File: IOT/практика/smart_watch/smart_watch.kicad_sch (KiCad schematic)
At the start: 30 parts, among them J1 Conn_01x02_Pin, J2 USB_C_Receptacle_USB2.0_16P, SW2 SW_Push, U1 WeMos_D1_mini, U3 KXTJ3-1057, U4 MAX30102, U5 TPS61230DRC, U6 BQ24090DGQ

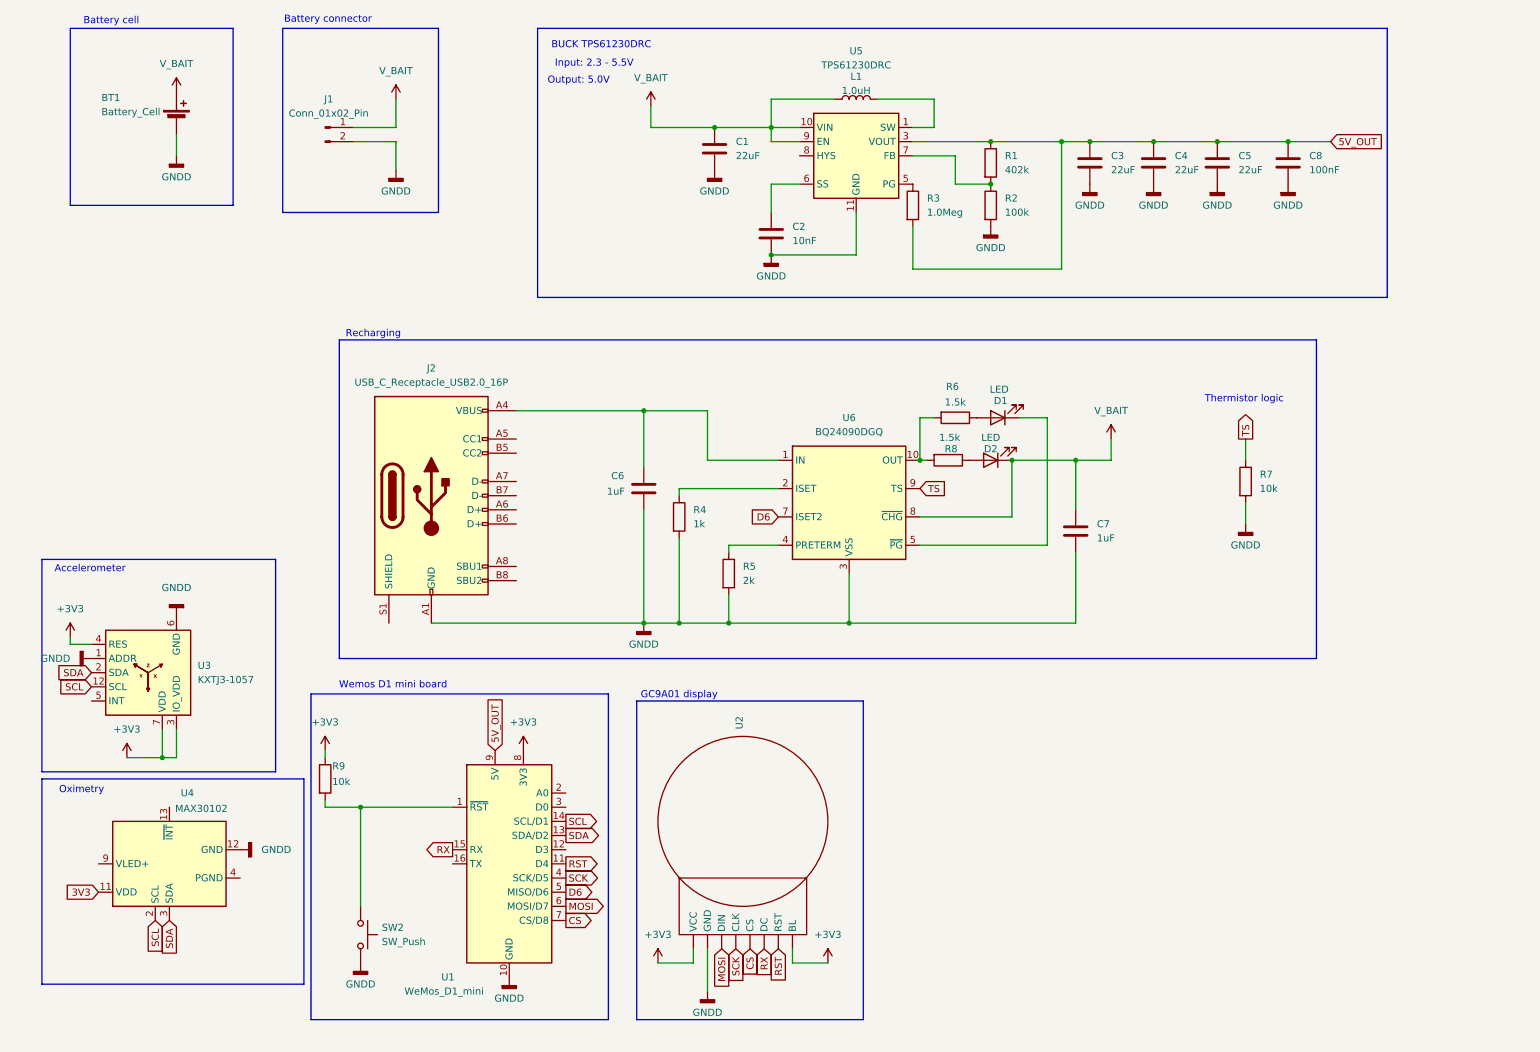
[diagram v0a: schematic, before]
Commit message: feat: adding hws and iot
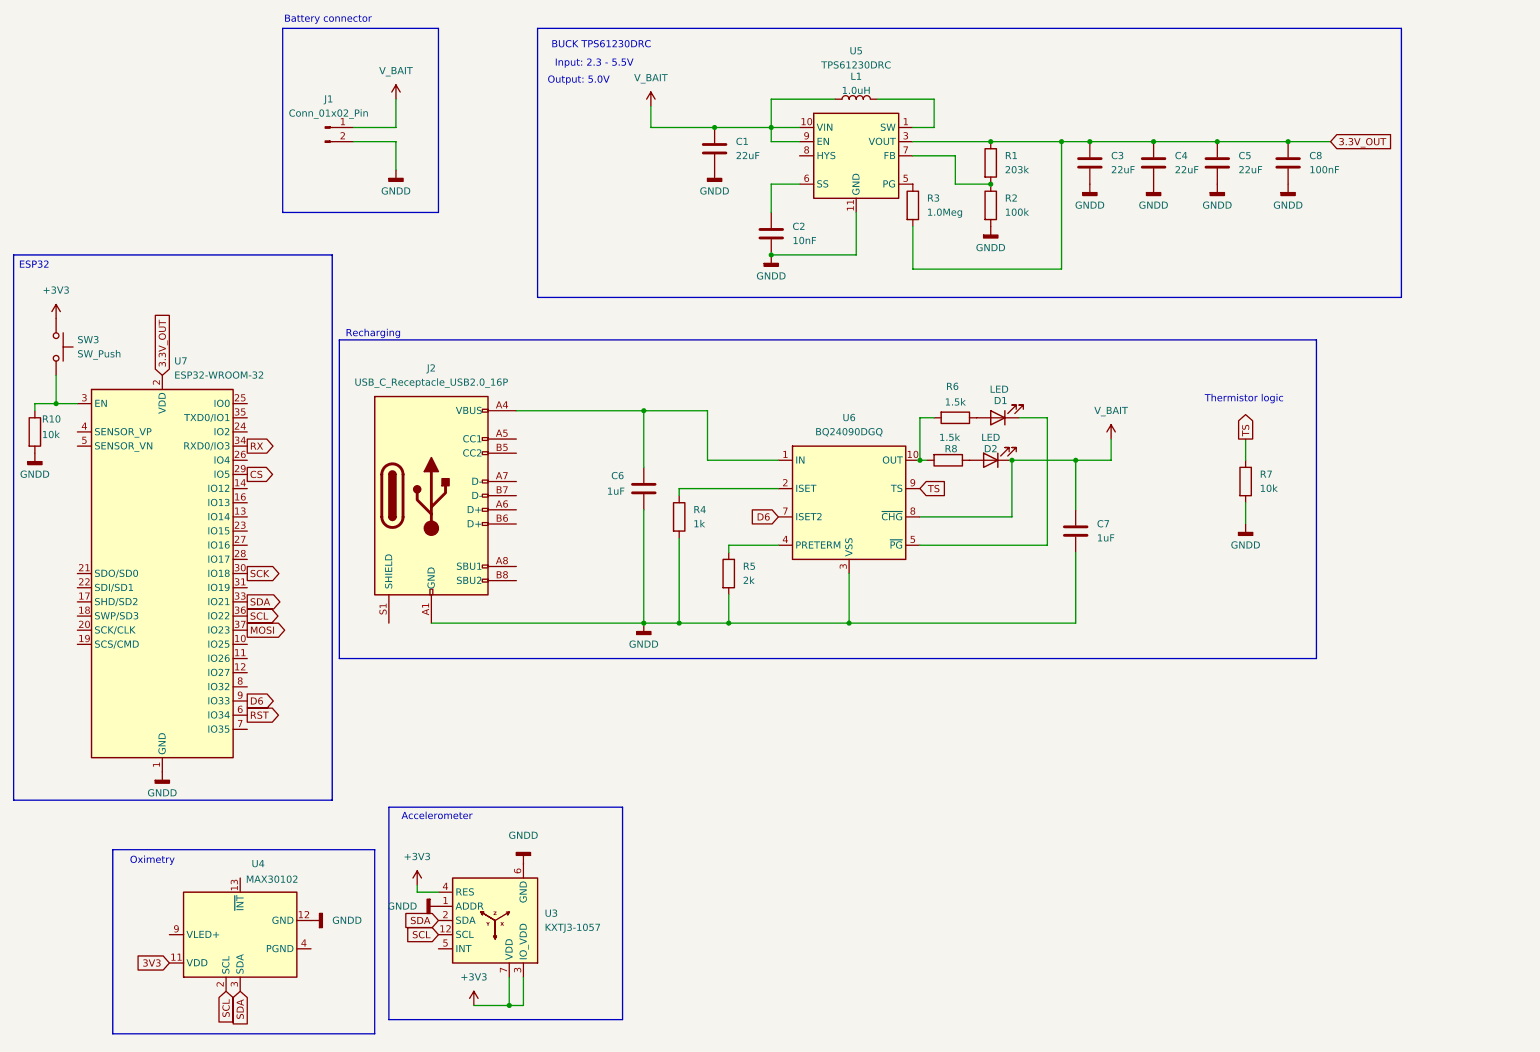
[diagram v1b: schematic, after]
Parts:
- removed BT1: Battery_Cell, symbol Device:Battery_Cell
- removed R9: 10k, Resistor_SMD:R_0402_1005Metric, symbol Device:R
- removed SW2: SW_Push, Button_Switch_SMD:SW_Push_1P1T_NO_CK_KMR2, symbol Switch:SW_Push
- removed U1: WeMos_D1_mini, Module:WEMOS_D1_mini_light, symbol MCU_Module:WeMos_D1_mini
- removed U2: ~, symbol circle_oled:Circle_OLED_gc9a01
- added R10: 10k, Resistor_SMD:R_0603_1608Metric, symbol Device:R
- added SW3: SW_Push, Button_Switch_SMD:SW_Push_1P1T_NO_CK_KMR2, symbol Switch:SW_Push
- added U7: ESP32-WROOM-32, RF_Module:ESP32-WROOM-32, symbol RF_Module:ESP32-WROOM-32
- C1, C2, C3, C4, C5, C6, C7, C8: footprint Capacitor_SMD:C_0805_2012Metric -> Capacitor_SMD:C_0603_1608Metric
- D1, D2: footprint LED_SMD:LED_0201_0603Metric -> LED_SMD:LED_0603_1608Metric
- J1: footprint (none) -> TerminalBlock:TerminalBlock_MaiXu_MX126-5.0-02P_1x02_P5.00mm
- L1: footprint Inductor_SMD:L_Coilcraft_LPS3314 -> Inductor_SMD:L_Changjiang_FXL0630
- R1: value 402k -> 203k; footprint Resistor_SMD:R_0402_1005Metric -> Resistor_SMD:R_0603_1608Metric
- R2, R3, R4, R5, R6, R7, R8: footprint Resistor_SMD:R_0402_1005Metric -> Resistor_SMD:R_0603_1608Metric
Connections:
- net +3V3: now also SW3.1
- net CS: now also U7.29 (IO5)
- net D6: now also U7.9 (IO33)
- net GNDD: now also R10.2, U7.1 (GND), U7.15 (GND), U7.38 (GND), U7.39 (GND)
- net MOSI: now also U7.37 (IO23)
- net RST: now also U7.6 (IO34)
- net RX: now also U7.34 (RXD0/IO3)
- net SCK: now also U7.30 (IO18)
- net SCL: now also U7.36 (IO22)
- net SDA: now also U7.33 (IO21)
- net 5V_OUT renamed 3.3V_OUT
- net 3.3V_OUT: now also U7.2 (VDD)
- new net: R10.1, SW3.2, U7.3 (EN)
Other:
- note removed: "Battery cell"
- note removed: "GC9A01 display"
- note removed: "Wemos D1 mini board"
- moved on the sheet: U3, U4

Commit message: feat: adding things
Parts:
- added U1: ~, Connector_FFC:Hirose_FH12-13S-0.5SH_1x13-1MP_P0.50mm_Horizontal, symbol FH12-13S-0.5SH(55):FH12-13S-0.5SH(55)
- added U2: MAX17261xxWL, Package_BGA:Maxim_WLP-9_1.595x1.415_Layout3x3_P0.4mm_Ball0.27mm_Pad0.25mm_NSMD, symbol Battery_Management:MAX17261xxWL
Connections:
- net 3.3V_OUT: now also U1.1
- net GNDD: now also U1.2, U1.MP
- net MOSI: now also U1.4
- net SCK: now also U1.5
- net SCL: now also U1.11
- net SDA: now also U1.10
- net LCD_BL: now reaches U7.13 (IO14)
- net LCD_BL: now also U1.9
- net LCD_DC: now reaches U7.14 (IO12)
- net LCD_DC: now also U1.7
- net LCD_RST: now reaches U7.16 (IO13)
- net LCD_RST: now also U1.8
- net TP_INT: now reaches U7.23 (IO15)
- net TP_INT: now also U1.12
- net TP_RST: now reaches U7.27 (IO16)
- net TP_RST: now also U1.13
- net MISO: now reaches U7.31 (IO19)
- net MISO: now also U1.3
- net CS renamed LCD_CS
- net LCD_CS: now also U1.6

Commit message: feat: adding things
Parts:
- removed U2: MAX17261xxWL, Package_BGA:Maxim_WLP-9_1.595x1.415_Layout3x3_P0.4mm_Ball0.27mm_Pad0.25mm_NSMD, symbol Battery_Management:MAX17261xxWL
- added U8: LC709203FQH-01TWG, Package_DFN_QFN:WDFN-8-1EP_4x3mm_P0.65mm_EP2.4x1.8mm, symbol Battery_Management:LC709203FQH-01TWG
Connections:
- net +3V3: now also R10.1; no longer SW3.1
- net GNDD: now also SW3.1; no longer R10.2
- net at SW3.2, U7.3 (EN): now also R10.2; no longer R10.1
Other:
- moved on the sheet: R10, SW3
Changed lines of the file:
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@@
 	(wire
 		(pts
+			(xy 16.51 100.33) (xy 16.51 105.41)
+		)
+		(stroke
+			(width 0)
+			(type default)
+		)
+	)
+	(wire
+		(pts
 			(xy 200.66 59.69) (xy 200.66 36.83)
 		)
@@
 	(wire
 		(pts
-			(xy 16.51 83.82) (xy 16.51 85.09)
-		)
-		(stroke
-			(width 0)
-			(type default)
-		)
-	)
-	(wire
-		(pts
 			(xy 175.26 86.36) (xy 175.26 93.98)
 		)
@@
 	(wire
 		(pts
-			(xy 20.32 78.74) (xy 20.32 83.82)
+			(xy 20.32 76.2) (xy 20.32 83.82)
 		)
 		(stroke
@@
 	(wire
 		(pts
+			(xy 16.51 83.82) (xy 16.51 90.17)
+		)
+		(stroke
+			(width 0)
+			(type default)
+		)
+	)
+	(wire
+		(pts
 			(xy 149.86 99.06) (xy 132.08 99.06)
 		)
@@
 	(symbol
 		(lib_id "Device:R")
-		(at 16.51 88.9 0)
+		(at 20.32 72.39 0)
 		(unit 1)
 		(exclude_from_sim no)
@@
 		(dnp no)
 		(property "Reference" "R10"
-			(at 17.78 86.614 0)
+			(at 21.59 70.104 0)
 			(effects
 				(font
@@
 		)
 		(property "Value" "10k"
-			(at 17.78 89.408 0)
+			(at 21.59 72.898 0)
 			(effects
 				(font
@@
 		)
 		(property "Footprint" "Resistor_SMD:R_0603_1608Metric"
-			(at 14.732 88.9 90)
+			(at 18.542 72.39 90)
 			(effects
 				(font
@@
 		)
 		(property "Datasheet" "~"
-			(at 16.51 88.9 0)
+			(at 20.32 72.39 0)
 			(effects
 				(font
@@
 		)
 		(property "Description" "Resistor"
-			(at 16.51 88.9 0)
+			(at 20.32 72.39 0)
 			(effects
 				(font
@@
 	)
 	(symbol
+		(lib_id "Battery_Management:LC709203FQH-01TWG")
+		(at 204.47 148.59 0)
+		(unit 1)
+		(exclude_from_sim no)
+		(in_bom yes)
+		(on_board yes)
+		(dnp no)
+		(fields_autoplaced yes)
+		(property "Reference" "U8"
+			(at 206.6133 133.35 0)
+			(effects
+				(font
+					(size 1.27 1.27)
+				)
+				(justify left)
+			)
+		)
+		(property "Value" "LC709203FQH-01TWG"
+			(at 206.6133 135.89 0)
+			(effects
+				(font
+					(size 1.27 1.27)
+				)
+				(justify left)
+			)
+		)
+		(property "Footprint" "Package_DFN_QFN:WDFN-8-1EP_4x3mm_P0.65mm_EP2.4x1.8mm"
+			(at 204.47 162.56 0)
+			(effects
+				(font
+					(size 1.27 1.27)
+				)
+				(hide yes)
+			)
+		)
+		(property "Datasheet" "https://www.onsemi.com/download/data-sheet/pdf/lc709203f-d.pdf"
+			(at 203.2 151.13 0)
+			(effects
+				(font
+					(size 1.27 1.27)
+				)
+				(hide yes)
+			)
+		)
+		(property "Description" "Single LiPo battery fuel gauge, I2C, type 01, WDFN-8"
+			(at 204.47 148.59 0)
+			(effects
+				(font
+					(size 1.27 1.27)
+				)
+				(hide yes)
+			)
+		)
+		(pin "8"
+		)
+		(pin "9"
+		)
+		(pin "6"
+		)
+		(pin "7"
+		)
+		(pin "5"
+		)
+		(pin "1"
+		)
+		(pin "3"
+		)
+		(pin "4"
+		)
+		(pin "2"
+		)
+		(instances
+			(project ""
+				(path "/f6146d92-14fa-4b9b-a242-2fe338df02db"
+					(reference "U8")
+					(unit 1)
+				)
+			)
+		)
+	)
+	(symbol
 		(lib_id "Device:LED")
 		(at 187.96 93.98 180)
@@
 	(symbol
 		(lib_id "Switch:SW_Push")
-		(at 20.32 73.66 270)
+		(at 16.51 95.25 90)
 		(unit 1)
 		(exclude_from_sim no)
@@
 		(fields_autoplaced yes)
 		(property "Reference" "SW3"
-			(at 24.13 72.3899 90)
+			(at 17.78 93.9799 90)
 			(effects
 				(font
 					(size 1.27 1.27)
 				)
-				(justify left)
+				(justify right)
 			)
 		)
 		(property "Value" "SW_Push"
-			(at 24.13 74.9299 90)
+			(at 17.78 96.5199 90)
 			(effects
 				(font
 					(size 1.27 1.27)
 				)
-				(justify left)
+				(justify right)
 			)
 		)
 		(property "Footprint" "Button_Switch_SMD:SW_Push_1P1T_NO_CK_KMR2"
-			(at 25.4 73.66 0)
+			(at 11.43 95.25 0)
 			(effects
 				(font
@@
 		)
 		(property "Datasheet" "~"
-			(at 25.4 73.66 0)
+			(at 11.43 95.25 0)
 			(effects
 				(font
@@
 		)
 		(property "Description" "Push button switch, generic, two pins"
-			(at 20.32 73.66 0)
+			(at 16.51 95.25 0)
 			(effects
 				(font
@@
 	(symbol
 		(lib_id "power:GNDD")
-		(at 16.51 92.71 0)
+		(at 16.51 105.41 0)
 		(unit 1)
 		(exclude_from_sim no)
@@
 		(fields_autoplaced yes)
 		(property "Reference" "#PWR029"
-			(at 16.51 99.06 0)
+			(at 16.51 111.76 0)
 			(effects
 				(font
@@
 		)
 		(property "Value" "GNDD"
-			(at 16.51 96.52 0)
+			(at 16.51 109.22 0)
 			(effects
 				(font
@@
 		)
 		(property "Footprint" ""
-			(at 16.51 92.71 0)
+			(at 16.51 105.41 0)
 			(effects
 				(font
@@
 		)
 		(property "Datasheet" ""
-			(at 16.51 92.71 0)
+			(at 16.51 105.41 0)
 			(effects
 				(font
@@
 		)
 		(property "Description" "Power symbol creates a global label with name \"GNDD\" , digital ground"
-			(at 16.51 92.71 0)
+			(at 16.51 105.41 0)
 			(effects
 				(font
@@
 					(unit 1)
 				)
-			)
-		)
-	)
-	(symbol
-		(lib_id "Battery_Management:MAX17261xxWL")
-		(at 205.74 149.86 0)
-		(unit 1)
-		(exclude_from_sim no)
-		(in_bom yes)
-		(on_board yes)
-		(dnp no)
-		(fields_autoplaced yes)
-		(property "Reference" "U2"
-			(at 207.8833 134.62 0)
-			(effects
-				(font
-					(size 1.27 1.27)
-				)
-				(justify left)
-			)
-		)
-		(property "Value" "MAX17261xxWL"
-			(at 207.8833 137.16 0)
-			(effects
-				(font
-					(size 1.27 1.27)
-				)
-				(justify left)
-			)
-		)
-		(property "Footprint" "Package_BGA:Maxim_WLP-9_1.595x1.415_Layout3x3_P0.4mm_Ball0.27mm_Pad0.25mm_NSMD"
-			(at 233.68 170.18 0)
-			(effects
-				(font
-					(size 1.27 1.27)
-				)
-				(hide yes)
-			)
-		)
-		(property "Datasheet" "https://datasheets.maximintegrated.com/en/ds/MAX17261.pdf"
-			(at 205.74 147.32 0)
-			(effects
-				(font
-					(size 1.27 1.27)
-				)
-				(hide yes)
-			)
-		)
-		(property "Description" "5.1μA Multi-Cell Fuel Gauge with ModelGauge m5 EZ, WLP-9"
-			(at 205.74 149.86 0)
-			(effects
-				(font
-					(size 1.27 1.27)
-				)
-				(hide yes)
-			)
-		)
-		(pin "B2"
-		)
-		(pin "B1"
-		)
-		(pin "C2"
-		)
-		(pin "C3"
-		)
-		(pin "A1"
-		)
-		(pin "A3"
-		)
-		(pin "C1"
-		)
-		(pin "A2"
-		)
-		(pin "B3"
-		)
-		(instances
-			(project ""
-				(path "/f6146d92-14fa-4b9b-a242-2fe338df02db"
-					(reference "U2")
-					(unit 1)
-				)

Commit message: updating smart watch
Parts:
- added C10, C9: 0.1 uF, Capacitor_SMD:C_0603_1608Metric, symbol Device:C
- added C16: 1uF, Capacitor_SMD:C_0603_1608Metric, symbol Device:C
- added R11, R12, R13, R14, R15, R16, R9: 10K, Resistor_SMD:R_0603_1608Metric, symbol Device:R
- added SW4: SW_Push, Button_Switch_SMD:SW_Push_1P1T_NO_CK_KMR2, symbol Switch:SW_Push
- added U10: NLSV2T244D, Package_SO:SOIC-8_3.9x4.9mm_P1.27mm, symbol Logic_LevelTranslator:NLSV2T244D
- added U2: CH330N, Package_SO:SOIC-8_3.9x4.9mm_P1.27mm, symbol Interface_USB:CH330N
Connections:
- net 3V3 is gone; now on net +3V3: U4.11 (VDD)
- net +3V3: now also R13.1, R14.1, R15.2, R16.2
- net GNDD: now also U8.1 (TEST), U8.2 (V_{SS}), C16.2, SW4.2, U10.4 (~{OE}), U10.5 (GND)
- net RX: now also U10.6 (B2)
- net SCL: now also U8.8 (SCL), R11.2, R13.2, R15.1
- net SDA: now also U8.7 (SDA), R14.2, R16.1, R9.2
- net TP_RST: now also U7.26 (IO4); no longer U7.27 (IO16)
- net V_BAIT: now also U8.3 (V_{DD}), C16.1, R12.1
- net VBUS: now reaches C6.1, J2.A4 (VBUS), J2.A9 (VBUS), J2.B4 (VBUS), J2.B9 (VBUS), U6.1 (IN)
- net VBUS: now also C10.1, U10.1 (VCCA), U2.5 (VCC)
- net BOOT: now reaches U7.25 (IO0)
- net BOOT: now also SW4.1
- net TX_2: now reaches U7.28 (IO17)
- net TX: now reaches U7.35 (TXD0/IO1)
- net TX: now also U10.7 (B1)
- net at U8.4 (~{ALARMB}): now also R12.2
- net D+: now reaches J2.A6 (D+)
- net D+: now also U2.1 (UD+)
- net D-: now reaches J2.A7 (D-)
- net D-: now also U2.2 (UD-)
- new net: U10.2 (A1), U2.6 (TXD)
- new net: U10.3 (A2), U2.7 (RXD)
- new net: C10.2, C9.1, U2.3 (GND)
- new net: C9.2, U2.8 (V3)
- new net +3.3V: R11.1, R9.1, U10.8 (VCCB)
- new net RX_2: U7.27 (IO16)
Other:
- moved on the sheet: C6, C7, D1, D2, J2, R4, R5, R6, R7, R8, U1, U3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

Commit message: updating smart watch
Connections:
- net RX_2: no longer names the net of U7.27 (IO16)
- net TX_2: no longer names the net of U7.28 (IO17)
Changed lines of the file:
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@@
-		)
-	)
-	(global_label "TX_2"
-		(shape output)
-		(at 54.61 111.76 0)
-		(fields_autoplaced yes)
-		(effects
-			(font
-				(size 1.27 1.27)
-			)
-			(justify left)
-		)
-		(property "Intersheetrefs" "${INTERSHEET_REFS}"
-			(at 61.9494 111.76 0)
-			(effects
-				(font
-					(size 1.27 1.27)
-				)
-				(justify left)
-				(hide yes)
-			)
 		)
 	)
@@
 			(effects
 				(font
-					(size 1.27 1.27)
-				)
-				(justify left)
-				(hide yes)
-			)
-		)
-	)
-	(global_label "RX_2"
-		(shape input)
-		(at 54.61 109.22 0)
-		(fields_autoplaced yes)
-		(effects
-			(font
-				(size 1.27 1.27)
-			)
-			(justify left)
-		)
-		(property "Intersheetrefs" "${INTERSHEET_REFS}"
-			(at 62.2518 109.22 0)
-			(effects
-				(font
